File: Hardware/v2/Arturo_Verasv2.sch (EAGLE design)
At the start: 31 parts, among them T3 2SC1815, T4 2SC1815, T6 2SC1815, T7 2SC1815

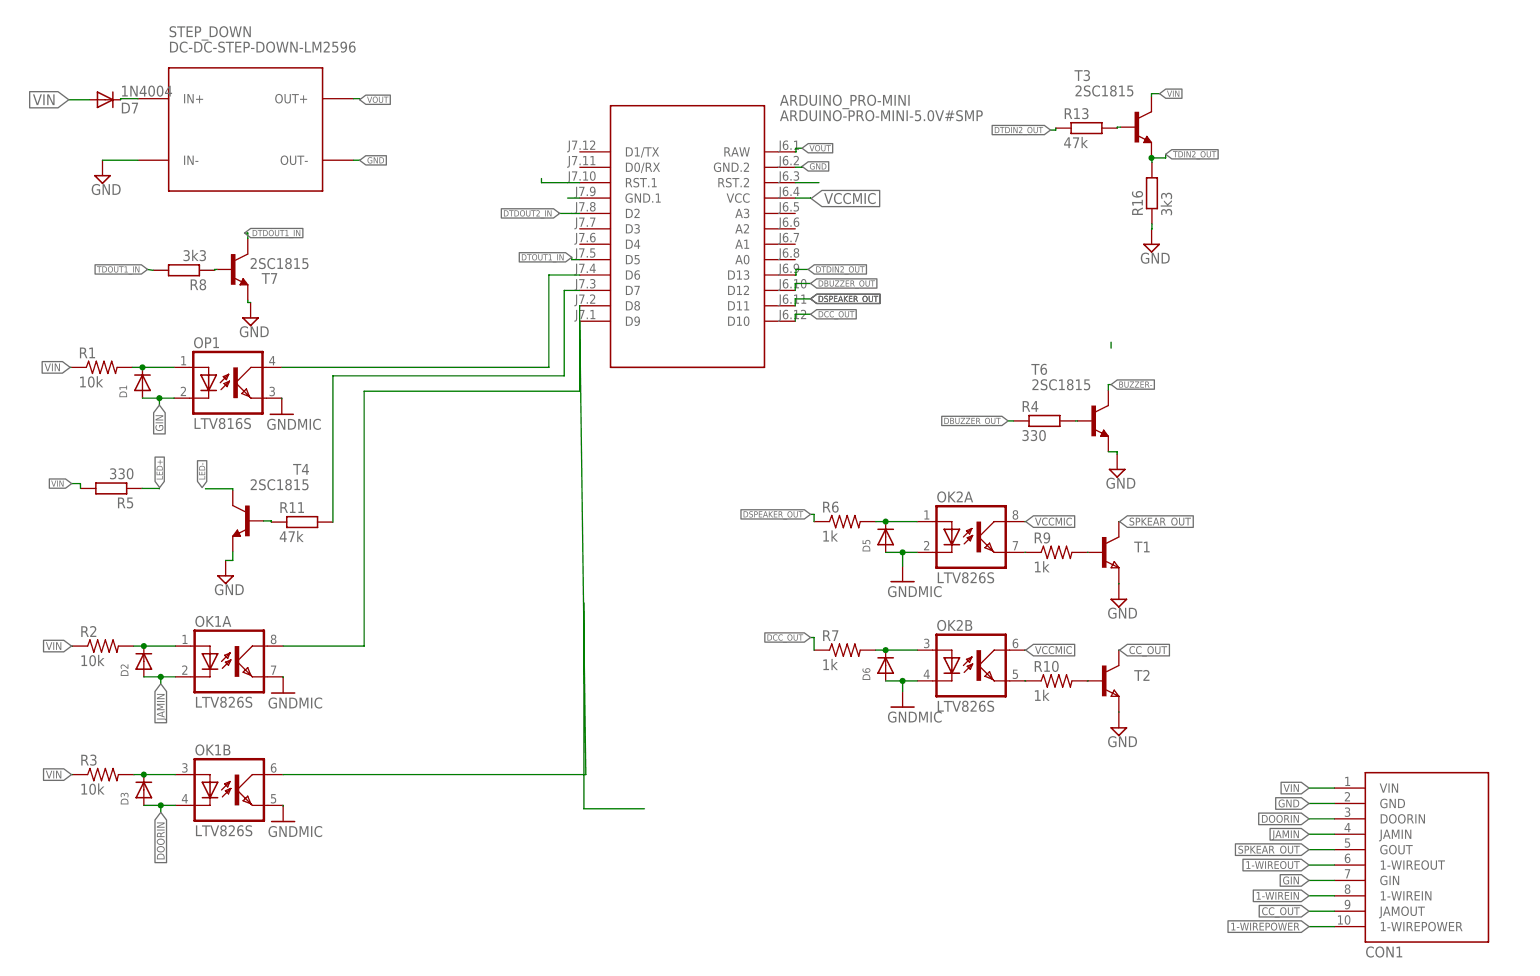
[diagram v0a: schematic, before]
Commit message: hardware update
se agregan más componentes
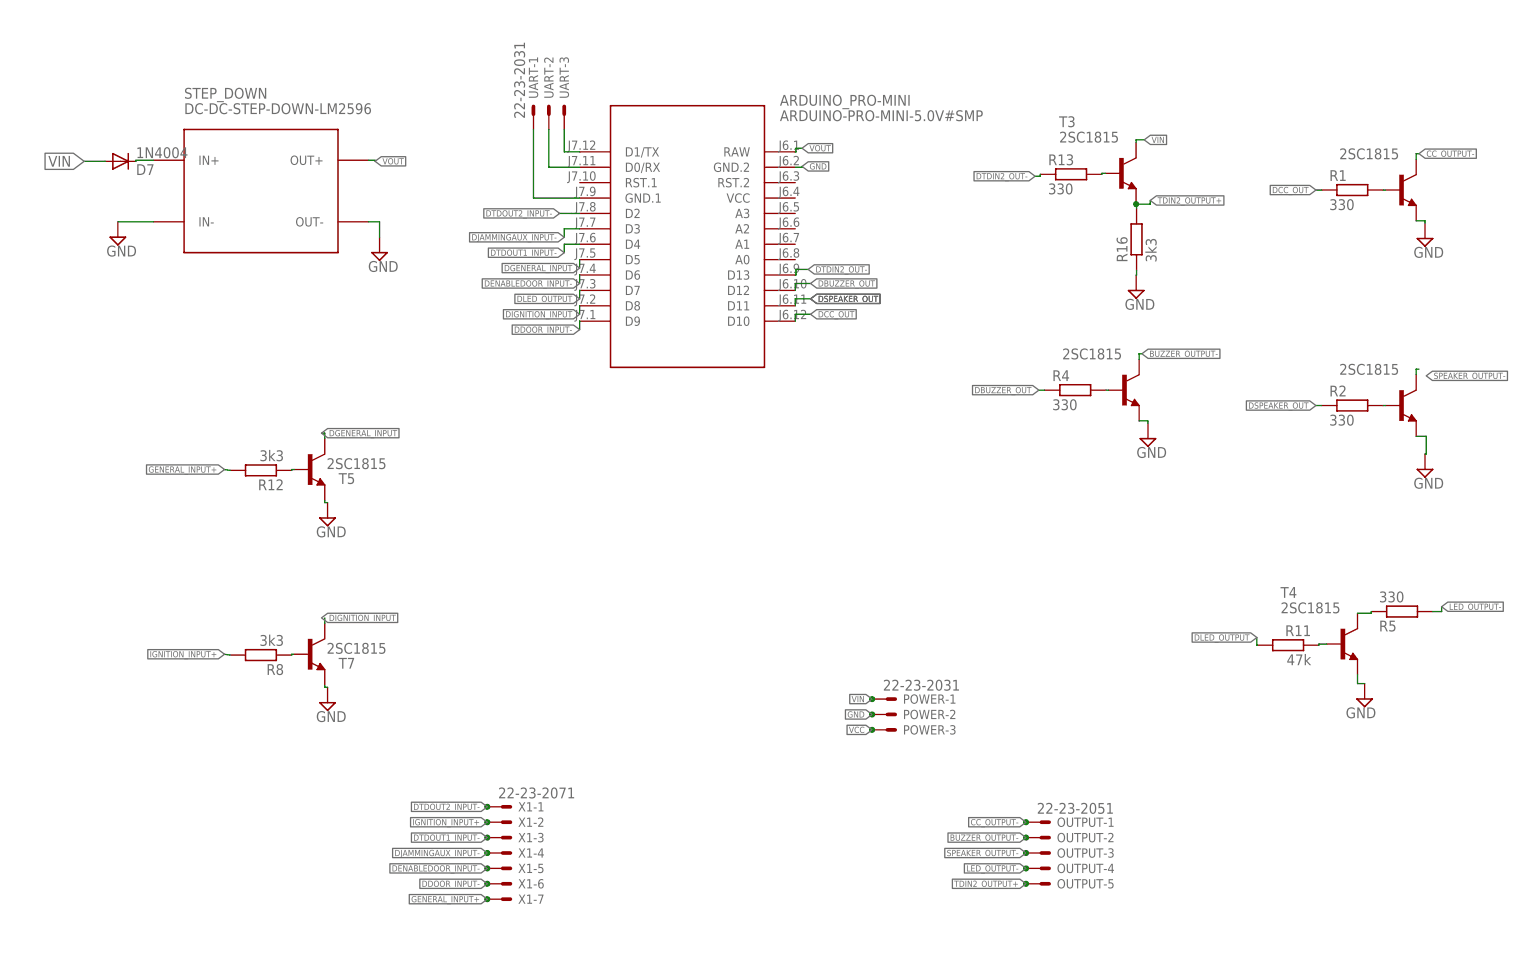
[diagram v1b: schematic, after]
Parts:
- removed CON1: (no value), ArturoVeras:TIN_HEADER_10POS
- removed D1, D2, D3, D5, D6: (no value), adafruit:DIODESOD-323F
- removed OK1, OK2: LTV826S, optocoupler:LTV826S
- removed OP1: LTV816S, ArturoVeras:LTV816S
- removed R10, R6, R7, R9: 1k, rcl:R-US_R0603
- removed R3: 10k, rcl:R-US_R0603
- removed T2: (no value), ArturoVeras:PBSS4360Z
- added OUTPUT: 22-23-2051, con-molex:22-23-2051
- added POWER, UART: 22-23-2031, con-molex:22-23-2031
- added R12: 3k3, resistor:R-EU_0204/7
- added T5, T8: 2SC1815, transistor:2SC1815
- added X1: 22-23-2071, con-molex:22-23-2071
- R1, R2: value 10k -> 330; device rcl:R-US_R0603 -> resistor:R-EU_0204/7
- R13: value 47k -> 330
- T1: value (none) -> 2SC1815; device ArturoVeras:PBSS4360Z -> transistor:2SC1815
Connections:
- net DTDIN2_OUT renamed DTDIN2_OUT-
- net N$21 renamed DLED_OUTPUT
- removed net 1-WIREIN: CON1.1-WIREIN
- removed net 1-WIREOUT: CON1.1-WIREOUT
- removed net 1-WIREPOWER: CON1.1-WIREPOWER
- removed net BUZZER-: T6.C
- removed net CC_OUT: CON1.JAMOUT, T2.C
- removed net DOORIN: CON1.DOORIN, D3.A, OK1B.C
- removed net DTDOUT1_IN: T7.C
- removed net DTDOUT2_IN: ARDUINO_PRO-MINI.D2
- removed net DTOUT1_IN: ARDUINO_PRO-MINI.D5
- removed net GIN: CON1.GIN, D1.A, OP1.C
- removed net GNDMIC: D5.A, D6.A, OK1A.EMIT, OK1B.EMIT, OK2A.C, OK2B.C, OP1.EMIT
- removed net JAMIN: CON1.JAMIN, D2.A, OK1A.C
- removed net LED+: R5.1
- removed net LED-: T4.C
- removed net N$10: ARDUINO_PRO-MINI.D9, OK1B.COL
- removed net N$11: OK2A.EMIT, R9.1
- removed net N$13: D5.C, OK2A.A, R6.2
- removed net N$15: D6.C, OK2B.A, R7.2
- removed net N$16: OK2B.EMIT, R10.1
- removed net N$17: R9.2, T1.B
- removed net N$18: R10.2, T2.B
- removed net N$24: ARDUINO_PRO-MINI.RST.2
- removed net SPKEAR_OUT: CON1.GOUT, T1.C
- removed net TDIN2_OUT: R16.2, T3.E
- removed net TDOUT1_IN: R8.2
- removed net VCCMIC: ARDUINO_PRO-MINI.VCC, OK2A.COL, OK2B.COL
- new net BUZZER_OUTPUT-: OUTPUT-2.S, T6.C
- new net CC_OUTPUT-: OUTPUT-1.S, T8.C
- new net DDOOR_INPUT-: ARDUINO_PRO-MINI.D9, X1-6.S
- new net DENABLEDOOR_INPUT-: ARDUINO_PRO-MINI.D6, X1-5.S
- new net DGENERAL_INPUT: ARDUINO_PRO-MINI.D5, T5.C
- new net DIGNITION_INPUT: ARDUINO_PRO-MINI.D8, T7.C
- new net DJAMMINGAUX_INPUT-: ARDUINO_PRO-MINI.D3, X1-4.S
- new net DTDOUT1_INPUT-: ARDUINO_PRO-MINI.D4, X1-3.S
- new net DTDOUT2_INPUT-: ARDUINO_PRO-MINI.D2, X1-1.S
- new net GENERAL_INPUT+: R12.2, X1-7.S
- new net IGNITION_INPUT+: R8.2, X1-2.S
- new net LED_OUTPUT-: OUTPUT-4.S, R5.2
- new net N$1: R12.1, T5.B
- new net SPEAKER_OUTPUT-: OUTPUT-3.S, T1.C
- new net TDIN2_OUTPUT+: OUTPUT-5.S, R16.2, T3.E
- new net VCC: POWER-3.S
- net DCC_OUT: now also R1.1; no longer R7.1
- net DSPEAKER_OUT: now also R2.1; no longer R6.1
- net GND: now also POWER-2.S, T5.E, T8.E; no longer ARDUINO_PRO-MINI.GND.1, CON1.GND, T2.E
- net N$3: now also R1.2, T8.B; no longer ARDUINO_PRO-MINI.D6, OP1.COL
- net N$4: now also R2.2, T1.B; no longer D1.C, OP1.A, R1.2
- net N$6: now also R5.1, T4.C; no longer D2.C, OK1A.A, R2.2
- net N$7: now also ARDUINO_PRO-MINI.D1/TX, UART-3.S; no longer ARDUINO_PRO-MINI.D8, OK1A.COL
- net N$8: now also ARDUINO_PRO-MINI.D0/RX, UART-2.S; no longer D3.C, OK1B.A, R3.2
- net N$9: now also ARDUINO_PRO-MINI.GND.1, UART-1.S; no longer ARDUINO_PRO-MINI.RST.1
- net VIN: now also POWER-1.S; no longer CON1.VIN, R1.1, R2.1, R3.1, R5.2
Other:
- moved on the sheet: D7, R11, R13, R16, R4, R5, R8, STEP_DOWN, T3, T4, T7
